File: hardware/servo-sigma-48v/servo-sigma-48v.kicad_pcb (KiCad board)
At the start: 4 copper layers, 72.7 x 75.2 mm, 205 parts, among them J1 CONN_01X02, J10 Conn_01x03, J11 Conn_01x03, J12 Conn_01x05, J2 CONN_02X05, J3 CONN_01X03, J4 Conn_01x03, J5 Conn_01x05, J6 629_105_150_921, J7 CONN_01X02, J8 Conn_01x03, J9 Conn_01x03, Q1 STL160NS3LLH7, Q2 STL160NS3LLH7, Q3 STL160NS3LLH7, Q4 STL160NS3LLH7, Q5 STL160NS3LLH7, Q6 STL160NS3LLH7, Q7 STL160NS3LLH7, Q8 STL160NS3LLH7, SW1 SW_DIP_x04, U1 ST1S14, U10 OPA4374, U11 L6398, U12 SN65HVD75DGKR, U2 TPS70950, U3 SN65HVD75DGKR, U4 L6398, U5 STM32F405VGTx, U6 L6398, U7 L6398, U8 TPS70933, U9 OPA4374, Y1 ABM3-8.000MHZ-D2Y-T

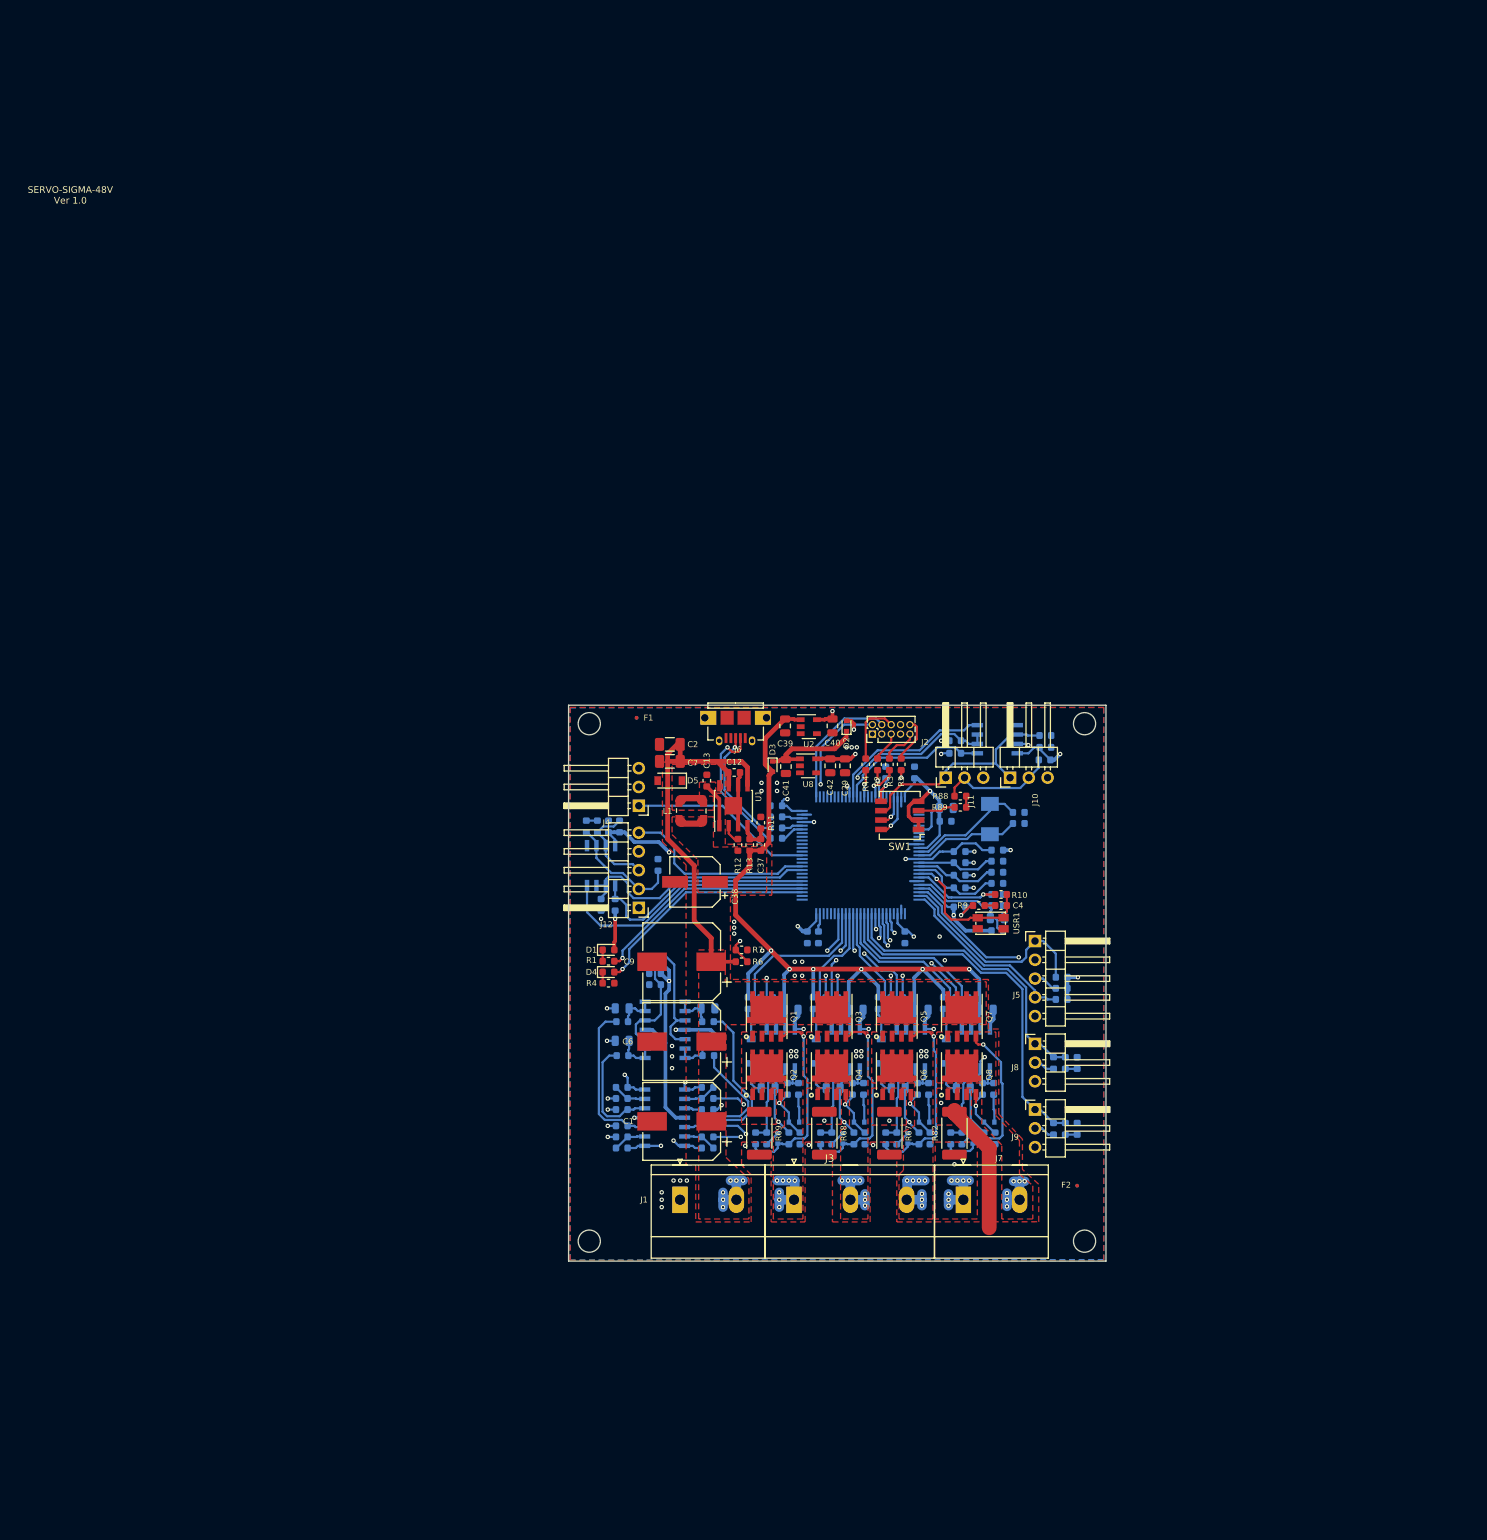
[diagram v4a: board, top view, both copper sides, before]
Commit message: Added NPTH for mounting heat sink.
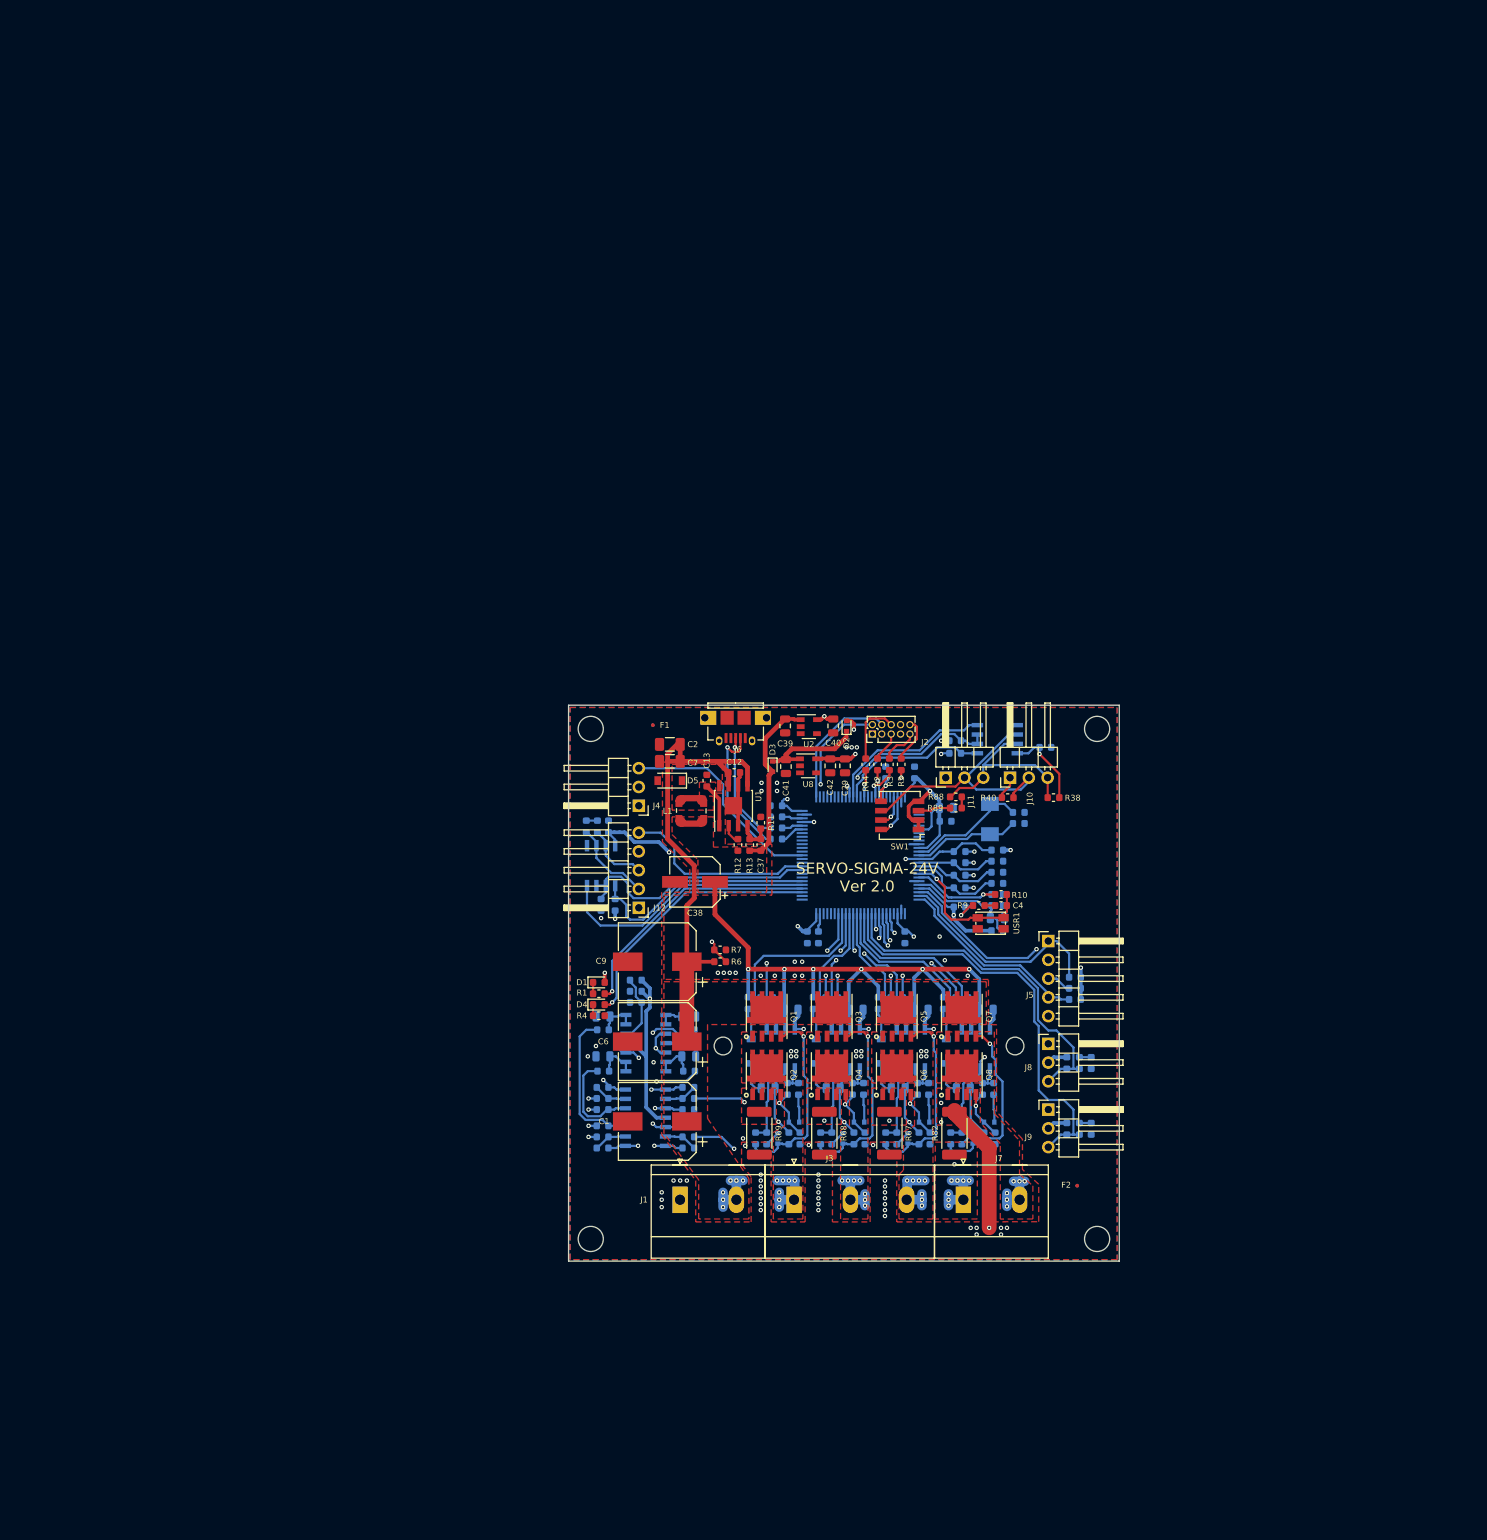
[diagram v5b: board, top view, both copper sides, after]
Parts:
- removed R86, R87: 4.7k, Resistor_SMD:R_0603_1608Metric
- R38, R40: value 4.7k -> N/A; moved to F.Cu
- moved R38 58.8 mm to (142.1, 58.4), turned to 0 degrees
- moved R40 48.2 mm to (135.9, 58.4), turned to 0 degrees
- moved D1 4.59 mm to (80.6, 83.4)
- moved D4 4.59 mm to (80.6, 86.4)
- moved R1 4.59 mm to (80.6, 84.9)
- moved R4 4.59 mm to (80.6, 87.9)
- moved R16 3.54 mm to (85.6, 83.1)
- moved C43 3.54 mm to (85.6, 84.6)
- moved R21 3.54 mm to (85.6, 86.1)
- moved C44 3.34 mm to (81.1, 93.4)
- moved R72 3.34 mm to (92.8, 95.4)
- moved C46 3.34 mm to (92.8, 93.4)
- moved R57 3.34 mm to (81.2, 95.4)
- moved C1 3.30 mm to (88.5, 102.2)
- moved C6 3.30 mm to (88.5, 91.4)
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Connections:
- J10 pad 1: /MCU/A_TERM_R120 -> GND
- J10 pad 2: Net-(J10-Pad2) -> /MCU/A_TERM_R120
- J10 pad 3: GND -> Net-(J10-Pad3)
- J11 pad 1: /MCU/A_TERM_R120 -> GND
- J11 pad 2: Net-(J10-Pad2) -> /MCU/A_TERM_R120
- J11 pad 3: GND -> Net-(J10-Pad3)
- J4 pad 1: /MCU/PWM -> GND
- J4 pad 3: GND -> /MCU/PWM
- J8 pad 1: /MCU/PB0 -> GND
- J8 pad 3: GND -> /MCU/PB0
- J9 pad 1: /MCU/PB1 -> GND
- J9 pad 3: GND -> /MCU/PB1
- R38 pad 1: Net-(J12-Pad3) -> Net-(J10-Pad3)
- R40 pad 2: Net-(J12-Pad2) -> /MCU/A_TERM_R120
- R88 pad 1: Net-(J10-Pad2) -> Net-(J10-Pad3)
- U12 pad 7: Net-(J10-Pad2) -> Net-(J10-Pad3)
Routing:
- net Net-(J10-Pad3): track 0.00 -> 25.2 mm
- net Net-(J10-Pad2): track 22.5 -> 0.00 mm, vias 1 -> 0
- net GND: track 219.1 -> 201.1 mm, vias 50 -> 77
- net VIN: track 63.5 -> 74.7 mm
- net +5V: track 175.8 -> 165.5 mm
- net Net-(R16-Pad1): track 31.9 -> 22.9 mm, vias 0 -> 2
- net /MCU/IC_FB: track 48.7 -> 56.4 mm
- net /MCU/PB1: track 49.0 -> 56.7 mm
- net /MCU/PB0: track 39.9 -> 47.0 mm
- net /MCU/IB_FB: track 58.7 -> 64.9 mm
- net /MCU/A_TERM_R120: track 31.1 -> 36.9 mm
- net /MOSFETs/B_ISENSE_P: track 16.3 -> 21.9 mm
- net Net-(R41-Pad2): track 18.6 -> 13.4 mm, vias 0 -> 2
- net /MCU/LED_STATUS: track 30.1 -> 35.0 mm
- net /MCU/LED_WARN: track 30.9 -> 35.9 mm
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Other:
- board size 72.7 x 75.2 mm -> 74.5 x 75.2 mm
- board text added: "SERVO-SIGMA-24V Ver 2.0"
- board text removed: "SERVO-SIGMA-48V Ver 1.0"

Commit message: Work on verson 2.0
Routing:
- net GND: track 201.1 -> 216.8 mm, vias 77 -> 74
- net /MOSFETs/R_ISENSE_P: track 61.3 -> 60.3 mm
- net /MOSFETs/C_ISENSE_P: track 7.02 -> 7.91 mm
- net /MOSFETs/A_ISENSE_P: track 47.6 -> 46.8 mm
- net /MOSFETs/B_ISENSE_P: track 21.9 -> 21.2 mm

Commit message: completed routing
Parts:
- removed C38: 100uF, Capacitor_SMD:CP_Elec_6.3x7.7
- removed C41, C47, C50: 1uF 100V, Capacitor_SMD:C_0805_2012Metric
- removed C42, C44, C45, C46: 4.7uF 25V, Capacitor_SMD:C_0805_2012Metric
- removed C43: 100nF 50V, Capacitor_SMD:C_0603_1608Metric
- removed C48, C49: 100pF 100V, Capacitor_SMD:C_0603_1608Metric
- removed D10, D12, D13, D15, D16, D6, D7, D9: BAT30KFILM, Diodes_SMD:D_SOD-523
- removed D11, D14, D17, D8: STPS0560Z, Diodes_SMD:D_SOD-123
- removed R21, R27, R32, R37, R42, R56, R79, R80: 10k, Resistor_SMD:R_0603_1608Metric
- removed R25, R26, R29, R35, R36, R39, R54, R55, R74, R75, R78: 5, Resistor_SMD:R_0603_1608Metric
- removed R31, R41, R59, R60, R63, R64, R70, R71: 1.0k 0.1%, Resistor_SMD:R_0603_1608Metric
- removed R33, R34, R43, R53, R76, R77, R89: 21, Resistor_SMD:R_0603_1608Metric
- removed R57, R58, R61, R62, R65, R66, R72, R73: 10k 0.1%, Resistor_SMD:R_0603_1608Metric
- removed R82: 0.010 1%, Resistor_SMD:R_2512_6332Metric
- removed U10, U9: OPA4374, Package_SO:SOIC-14_3.9x8.7mm_P1.27mm
- removed U11, U4, U6, U7: L6398, Package_SO:SOIC-8_3.9x4.9mm_P1.27mm
- removed U8: TPS70933, Package_TO_SOT_SMD:SOT-23-5
- added L2: 22uH, Inductor_SMD:L_Wuerth_WE-TPC-3816, F.Cu at (100.5, 64.1)
- added NT1: Net-Tie_2, NetTie:NetTie-2_SMD_Pad0.5mm, F.Cu at (80.5, 73.2)
- added NT2: Net-Tie_2, NetTie:NetTie-2_SMD_Pad0.5mm, F.Cu at (94.4, 90.6)
- added NT4: Net-Tie_2, NetTie:NetTie-2_SMD_Pad0.5mm, F.Cu at (110.8, 90.6)
- added NT6: Net-Tie_2, NetTie:NetTie-2_SMD_Pad0.5mm, F.Cu at (120.4, 90.6)
- C1, C6: value 120uF -> 4.7uF 50V; footprint Capacitor_SMD:CP_Elec_10x10 -> Capacitor_SMD:C_0805_2012Metric
- C11: value 4.7uF 25V -> 1uF 100V; footprint Capacitor_SMD:C_0805_2012Metric -> Capacitor_SMD:C_1206_3216Metric; moved to F.Cu
- C12: value 100nF 100V -> 100nF
- C13: value 100nF 50V -> 1uF 16V
- C16, C21: value 100pF 100V -> 0.047uF 100V; footprint Capacitor_SMD:C_0603_1608Metric -> Capacitor_SMD:C_0805_2012Metric; moved to F.Cu
- C17: value 1uF 100V -> 4.7uF 50V; moved to F.Cu
- C18, C33: value 100pF 100V -> 1uF 16V; moved to F.Cu
- C2, C7: value 10uF 50V -> 100nF; footprint Capacitor_SMD:C_1206_3216Metric -> Capacitor_SMD:C_0603_1608Metric
- C20: value 1uF 100V -> 1uF 16V; footprint Capacitor_SMD:C_0805_2012Metric -> Capacitor_SMD:C_0603_1608Metric; moved to F.Cu
- C22, C34: value 1uF 100V -> 100nF; footprint Capacitor_SMD:C_0805_2012Metric -> Capacitor_SMD:C_0603_1608Metric; moved to F.Cu
- C23: value 100pF 100V -> 4.7uF 50V; footprint Capacitor_SMD:C_0603_1608Metric -> Capacitor_SMD:C_0805_2012Metric; moved to F.Cu
- C26: value 1uF 100V -> 100uF; footprint Capacitor_SMD:C_0805_2012Metric -> Capacitor_SMD:CP_Elec_6.3x7.7; moved to F.Cu
- C35: value 100pF 100V -> 100uF; footprint Capacitor_SMD:C_0603_1608Metric -> Capacitor_SMD:CP_Elec_6.3x7.7; moved to F.Cu
- C36: value 1uF 100V -> 120uF; footprint Capacitor_SMD:C_0805_2012Metric -> Capacitor_SMD:CP_Elec_10x10; moved to F.Cu
- C37: value 820pF/50V/10% -> 120uF; footprint Capacitor_SMD:C_0603_1608Metric -> Capacitor_SMD:CP_Elec_10x10
- C39: footprint Capacitor_SMD:C_0805_2012Metric -> Capacitor_SMD:C_1206_3216Metric
- C40: value 4.7uF 25V -> 1uF 100V; footprint Capacitor_SMD:C_0805_2012Metric -> Capacitor_SMD:C_1206_3216Metric
- C9: value 120uF -> 100nF; footprint Capacitor_SMD:CP_Elec_10x10 -> Capacitor_SMD:C_0603_1608Metric
- D2, D3: value BAT30KFILM -> STPS0560Z; footprint Diodes_SMD:D_SOD-523 -> Diode_SMD:D_SOD-123
- D5: value STPS0560Z -> BAT30KFILM; footprint Diodes_SMD:D_SOD-123 -> Diode_SMD:D_SOD-523
- L1: value 8.2uH -> 22uH
- R11: value 2.7k -> 21
- R12: value 47k -> 21
- R13: value 30k -> 28k
- R16: value 10k -> 8.45k; moved to F.Cu
- R18: value 5 -> 18k; moved to F.Cu
- R22: value 10k -> 3.3k; moved to F.Cu
- R23: value 21 -> 47k; moved to F.Cu
- R24: value 21 -> 4.7k; moved to F.Cu
- R6: value 47k -> 10k
- R7: value 4.7k -> 10k
- U1: value ST1S14 -> DRV8323RS; footprint Package_SO:SOIC-8-1EP_3.9x4.9mm_P1.27mm_EP2.35x2.35mm -> Package_DFN_QFN:QFN-48-1EP_7x7mm_P0.5mm_EP5.45x5.45mm_ThermalVias
- U2: value TPS70950 -> DRV8323RS; footprint Package_TO_SOT_SMD:SOT-23-5 -> Package_DFN_QFN:QFN-48-1EP_7x7mm_P0.5mm_EP5.45x5.45mm_ThermalVias
- moved F2 97.7 mm to (85.7, 33.5)
- moved F4 97.7 mm to (85.7, 33.5)
- moved R30 81.1 mm to (80.6, 57.0), turned to 90 degrees
- moved F1 80.9 mm to (140.0, 110.5)
- moved F3 80.9 mm to (140.0, 110.5)
- moved C52 78.4 mm to (82.2, 57.0), turned to 90 degrees
- moved R28 75.7 mm to (83.9, 57.0), turned to 90 degrees
- moved R20 72.4 mm to (80.6, 65.9), turned to 90 degrees
- moved C51 69.5 mm to (82.2, 65.9), turned to 90 degrees
- moved J9 69.3 mm to (86.4, 58.4), turned to 180 degrees
- moved R17 66.4 mm to (83.9, 65.9), turned to 90 degrees
- moved J8 60.2 mm to (86.4, 67.3), turned to 180 degrees
- moved C2 54.4 mm to (136.0, 80.5), turned to 0 degrees
- moved C39 43.0 mm to (114.1, 90.9)
- moved C40 42.5 mm to (117.2, 90.9)
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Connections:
- C1 pad 2: GND -> PGND
- C11 pad 1: GND -> VIN
- C11 pad 2: Net-(C11-Pad2) -> PGND
- C12 pad 2: GND -> PGND
- C13 pad 1: Net-(C13-Pad1) -> VIN
- C16 pad 1: GND -> Net-(C16-Pad1)
- C16 pad 2: /MCU/PWM_CL -> Net-(C16-Pad2)
- C17 pad 1: /MOSFETs/PHASE_C -> VIN
- C17 pad 2: Net-(C17-Pad2) -> GND
- C18 pad 1: GND -> Net-(C18-Pad1)
- C18 pad 2: /MCU/PWM_CH -> GND
- C2 pad 1: VIN -> +3V3
- C20 pad 1: GND -> VIN
- C20 pad 2: +15V -> Net-(C20-Pad2)
- C21 pad 1: GND -> Net-(C21-Pad1)
- C21 pad 2: /MCU/PWM_BL -> Net-(C21-Pad2)
- C22 pad 1: /MOSFETs/PHASE_B -> Net-(C22-Pad1)
- C23 pad 1: GND -> +5V
- C23 pad 2: /MCU/PWM_BH -> GND
- C26 pad 1: GND -> +5V
- C26 pad 2: +15V -> GND
- C33 pad 1: GND -> Net-(C33-Pad1)
- C33 pad 2: /MCU/PWM_AL -> GND
- C34 pad 1: /MOSFETs/PHASE_A -> Net-(C34-Pad1)
- C35 pad 1: GND -> +3V3
- C35 pad 2: /MCU/PWM_AH -> GND
- C36 pad 1: GND -> VIN
- C36 pad 2: +15V -> PGND
- C37 pad 1: +15V -> VIN
- C37 pad 2: Net-(C37-Pad2) -> PGND
- C39 pad 1: GND -> VIN
- C39 pad 2: +15V -> PGND
- C4 pad 2: /MCU/PC3 -> /MCU/PD11
- C40 pad 1: GND -> VIN
- C40 pad 2: +5V -> PGND
- C51 pad 2: /MCU/PB0 -> /MCU/PB12
- C52 pad 2: /MCU/PB1 -> /MCU/PB13
- C6 pad 2: GND -> PGND
- C7 pad 1: VIN -> +3V3
- C9 pad 2: GND -> PGND
- D2 pad 1: Net-(C41-Pad2) -> Net-(C34-Pad2)
- D2 pad 2: /MCU/EXT_5V -> GND
- D3 pad 1: Net-(C41-Pad2) -> Net-(C22-Pad2)
- D3 pad 2: +15V -> GND
- D5 pad 1: Net-(C13-Pad2) -> +5V
- D5 pad 2: GND -> /MCU/EXT_5V
- J1 pad 1: GND -> PGND
- J3 pad 1: /MOSFETs/PHASE_C -> /MOSFETs/PHASE_A
- J3 pad 3: /MOSFETs/PHASE_A -> /MOSFETs/PHASE_C
- J4 pad 3: /MCU/PWM -> /MCU/PB4
- J7 pad 1: /MOSFETs/R_ISENSE_P -> PGND
- J8 pad 3: /MCU/PB0 -> /MCU/PB12
- J9 pad 3: /MCU/PB1 -> /MCU/PB13
- L1 pad 1: Net-(C13-Pad2) -> Net-(C34-Pad2)
- L1 pad 2: +15V -> +3V3
- Q1 pad 2: Net-(D10-Pad2) -> /MOSFETs/GHC
- Q2 pad 2: Net-(D9-Pad2) -> /MOSFETs/GLC
- Q3 pad 2: Net-(D13-Pad2) -> /MOSFETs/GHB
- Q4 pad 2: Net-(D12-Pad2) -> /MOSFETs/GLB
- Q5 pad 2: Net-(D16-Pad2) -> /MOSFETs/GHA
- Q6 pad 2: Net-(D15-Pad2) -> /MOSFETs/GLA
- Q7 pad 2: Net-(D6-Pad2) -> /MOSFETs/GHR
- Q8 pad 1: GND -> PGND
- Q8 pad 2: Net-(D7-Pad2) -> /MOSFETs/GLR
- R10 pad 2: /MCU/PC3 -> /MCU/PD11
- R11 pad 1: GND -> /MCU/DRV_SDO
- R11 pad 2: Net-(C37-Pad2) -> Net-(R11-Pad2)
- R12 pad 1: Net-(R12-Pad1) -> /MCU/DRV_SDO
- R12 pad 2: +15V -> Net-(R12-Pad2)
- R13 pad 1: Net-(C37-Pad2) -> Net-(R13-Pad1)
- R13 pad 2: +15V -> +3V3
- R16 pad 1: Net-(R16-Pad1) -> GND
- R16 pad 2: +3V3 -> Net-(R13-Pad1)
- R17 pad 2: /MCU/PB0 -> /MCU/PB12
- R18 pad 1: +15V -> Net-(R18-Pad1)
- R18 pad 2: Net-(D8-Pad2) -> +5V
- R22 pad 1: Net-(D10-Pad2) -> GND
- R22 pad 2: /MOSFETs/PHASE_C -> Net-(R18-Pad1)
- R23 pad 1: /MOSFETs/GATE_CL -> VIN
- R23 pad 2: Net-(D9-Pad2) -> /MCU/VBAT_ADC
- R24 pad 1: /MOSFETs/GATE_CH -> /MCU/VBAT_ADC
- R24 pad 2: Net-(D10-Pad2) -> GND
- R28 pad 2: /MCU/PB1 -> /MCU/PB13
- R6 pad 1: VIN -> +3V3
- R6 pad 2: /MCU/VBAT_ADC -> /MCU/DRV_SDO
- R67 pad 2: GND -> PGND
- R68 pad 2: GND -> PGND
- R69 pad 2: GND -> PGND
- R7 pad 1: /MCU/VBAT_ADC -> +3V3
- R7 pad 2: GND -> /MCU/DRV_FAULT
- R88 pad 2: Net-(R88-Pad2) -> /MCU/B_TERM_R120
- U1 pad 1: Net-(C13-Pad1) -> Net-(R13-Pad1)
- U1 pad 2: Net-(R12-Pad1) -> PGND
- U1 pad 3: GND -> Net-(C21-Pad2)
- U1 pad 4: Net-(C37-Pad2) -> Net-(C21-Pad1)
- U1 pad 5: VIN -> Net-(C20-Pad2)
- U1 pad 6: GND -> VIN
- U1 pad 8: Net-(C13-Pad2) -> Net-(U1-Pad8)
- U1 pad 9: GND -> Net-(U1-Pad9)
- U2 pad 1: +15V -> Net-(R18-Pad1)
- U2 pad 2: GND -> PGND
- U2 pad 3: Net-(U2-Pad3) -> Net-(C16-Pad2)
- U2 pad 4: Net-(U2-Pad4) -> Net-(C16-Pad1)
- U2 pad 5: +5V -> Net-(C13-Pad2)
- U5 pad 26: /MCU/PA3 -> /MCU/DRV2_CS
- U5 pad 29: /MCU/PA4 -> /MCU/DRV1_CS
- U5 pad 30: /MCU/IA_FB -> /MOSFETs/DRV_SOC
- U5 pad 31: /MCU/IB_FB -> /MOSFETs/DRV_SOB
- U5 pad 32: /MCU/IC_FB -> /MOSFETs/DRV_SOA
- U5 pad 33: /MCU/IR_FB -> /MCU/DRV_FAULT
- U5 pad 45: /MCU/PE14 -> /MCU/GATE_ENABLE
- U5 pad 46: /MCU/PE15 -> /MCU/DRV_CAL
- U5 pad 53: /MCU/LED_WARN -> /MCU/PB14
- U5 pad 54: /MCU/LED_STATUS -> /MCU/PB15
- U5 pad 61: /MCU/PD14 -> /MCU/LED_WARN
- U5 pad 62: /MCU/PD15 -> /MCU/LED_STATUS
- U5 pad 63: /MCU/PWM -> /MCU/PC6
- U5 pad 78: /MCU/PC10 -> /MCU/DRV_CLK
- U5 pad 79: /MCU/PC11 -> /MCU/DRV_SDO
- U5 pad 80: /MCU/PC12 -> /MCU/DRV_SDI
- USR1 pad 2: /MCU/PC3 -> /MCU/PD11
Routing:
- net GND: track 216.8 -> 95.6 mm, vias 74 -> 15
- net +15V: track 119.4 -> 0.00 mm, vias 6 -> 0
- net /MCU/DRV_CLK: track 0.00 -> 71.5 mm, vias 0 -> 3
- net /MCU/DRV_SDI: track 0.00 -> 69.2 mm, vias 0 -> 3
- net /MCU/IB_FB: track 64.9 -> 0.00 mm, vias 2 -> 0
- net /MCU/IR_FB: track 62.8 -> 0.00 mm, vias 2 -> 0
- net /MOSFETs/R_ISENSE_P: track 60.3 -> 0.00 mm, vias 9 -> 0
- net /MCU/PB1: track 56.7 -> 0.00 mm
- net /MCU/GATE_ENABLE: track 0.00 -> 56.6 mm, vias 0 -> 4
- net /MCU/IC_FB: track 56.4 -> 0.00 mm, vias 2 -> 0
- net /MCU/IA_FB: track 56.0 -> 0.00 mm, vias 2 -> 0
- net VIN: track 74.7 -> 126.3 mm, vias 6 -> 38
- net /MCU/PB0: track 47.0 -> 0.00 mm
- net Net-(R12-Pad2): track 0.00 -> 42.0 mm, vias 0 -> 2
- net +5V: track 165.5 -> 203.6 mm, vias 1 -> 5
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- added copper zone on F.Cu, net +3V3
- added copper zone on F.Cu, net +5V
- added copper zone on B.Cu, net /MOSFETs/PHASE_A
- added copper zone on In2.Cu, net /MOSFETs/PHASE_A
- added copper zone on B.Cu, net /MOSFETs/PHASE_B
- added copper zone on In2.Cu, net /MOSFETs/PHASE_B
- added copper zone on B.Cu, net /MOSFETs/PHASE_C
- added copper zone on In2.Cu, net /MOSFETs/PHASE_C
- added copper zone on B.Cu, net /MOSFETs/PHASE_R
- added copper zone on In1.Cu, net /MOSFETs/PHASE_R
- added copper zone on In2.Cu, net /MOSFETs/PHASE_R
- added copper zone on In1.Cu, net GND
- added copper zone on In2.Cu, net GND
- added copper zone on F.Cu, net Net-(C22-Pad2)
- added copper zone on F.Cu, net Net-(C34-Pad2)
- added copper zone on B.Cu, net PGND
- added copper zone on F.Cu, net PGND
- added copper zone on In1.Cu, net PGND
- added copper zone on In2.Cu, net PGND
- added copper zone on B.Cu, net VIN
- added copper zone on In1.Cu, net VIN
- added copper zone on In2.Cu, net VIN
- removed copper zone on F.Cu, net +15V
- removed copper zone on F.Cu, net /MOSFETs/R_ISENSE_P
- removed copper zone on F.Cu, net Net-(C13-Pad2)
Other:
- board size 74.5 x 75.2 mm -> 72 x 87.3 mm
- board text added: "+"
- board text added: "-"
- board text added: "48V"
- board text added: "BREAK"
- board text added: "SIGMADRIVE-48V Ver 3.0"
- board text added: "STAT"
- board text added: "U"
- board text added: "V"
- board text added: "W"
- board text added: "WARN"
- board text removed: "SERVO-SIGMA-24V Ver 2.0"
